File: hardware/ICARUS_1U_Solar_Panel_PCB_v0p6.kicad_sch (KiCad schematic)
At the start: 13 parts, among them J1 Molex_53398-0471

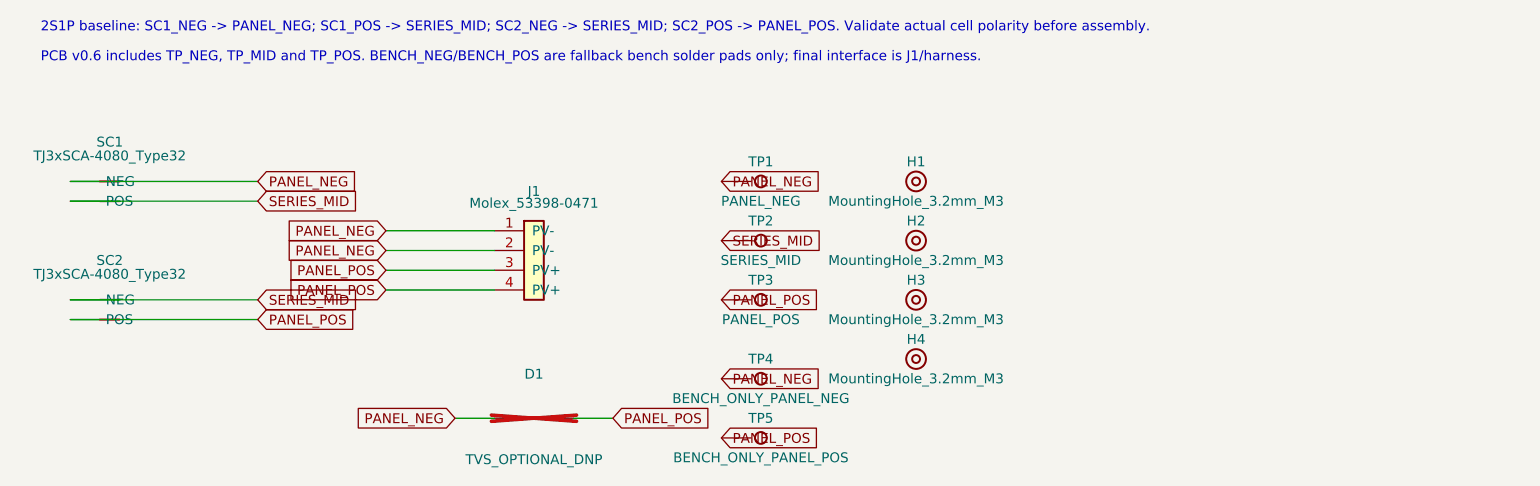
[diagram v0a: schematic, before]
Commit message: Repo hygiene: drop dead NC net, unify fp-lib-table, remove obsolete macOS reports
- Drop unused (net 4 "NC") from PCB (was declared but referenced by no
  pad/track).
- Point fp-lib-table entry for ICARUS_Connector at the unified
  hardware/footprints/ tree (matches ICARUS_Solar location).
- Update bench-pad note in schematic to use the real net names
  (BENCH_ONLY_PANEL_NEG/POS) instead of the old short forms.
- Delete the three .rpt files left from the aborted macOS DRC/ERC runs
  (DRC_v0p6.rpt, DRC_v0p6_layout_only.rpt, ERC_v0p6.rpt); current
  reports live in *_kicad10_win.rpt.

DRC parity remains clean (0 errors / 0 unconnected / 0 parity issues;
13 warnings = library-mismatch waived).

Co-Authored-By: Claude Opus 4.7 <noreply@anthropic.com>
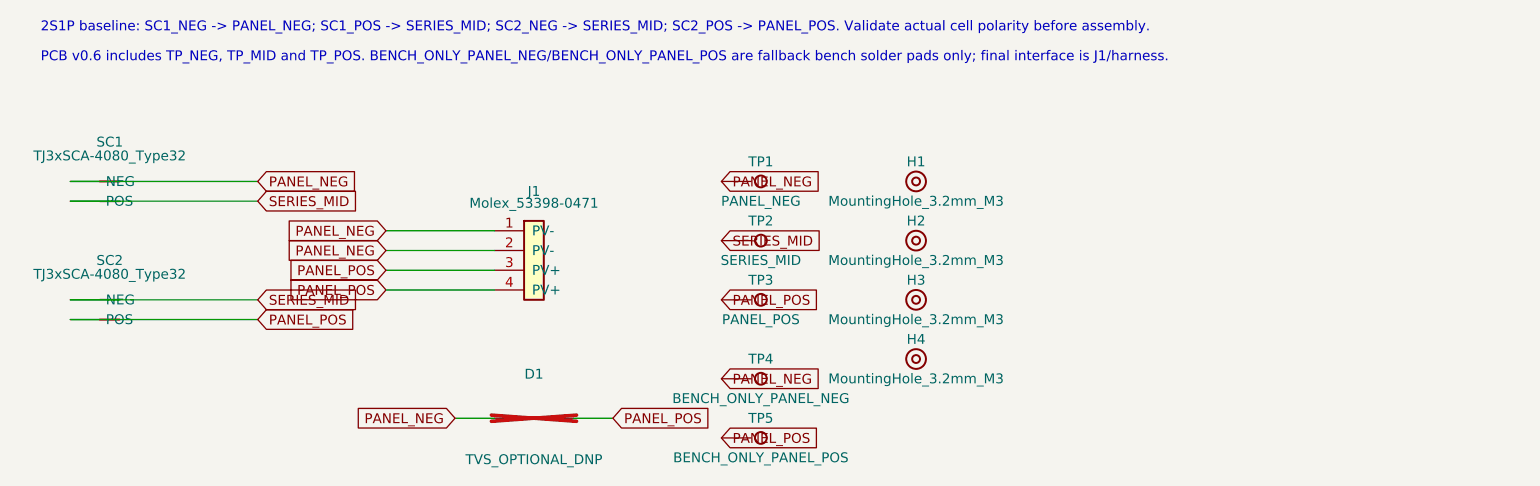
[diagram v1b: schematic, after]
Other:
- note added: "PCB v0.6 includes TP_NEG, TP_MID and TP_POS. BENCH_ONLY_PANEL_NEG/BENCH_ONLY_PANEL_POS are fallback bench solder pads only; final interface is J1/harness."
- note removed: "PCB v0.6 includes TP_NEG, TP_MID and TP_POS. BENCH_NEG/BENCH_POS are fallback bench solder pads only; final interface is J1/harness."
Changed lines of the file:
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@@
 			(global_label "PANEL_POS" (shape input) (at 154.94 109.22 0) (fields_autoplaced) (effects (font (size 1.27 1.27)) (justify left)))
 		(text "2S1P baseline: SC1_NEG -> PANEL_NEG; SC1_POS -> SERIES_MID; SC2_NEG -> SERIES_MID; SC2_POS -> PANEL_POS. Validate actual cell polarity before assembly." (at 67.31 57.15 0) (effects (font (size 1.27 1.27)) (justify left bottom)))
-	(text "PCB v0.6 includes TP_NEG, TP_MID and TP_POS. BENCH_NEG/BENCH_POS are fallback bench solder pads only; final interface is J1/harness." (at 67.31 61.0 0) (effects (font (size 1.27 1.27)) (justify left bottom)) (uuid "bench-note-v05"))
+	(text "PCB v0.6 includes TP_NEG, TP_MID and TP_POS. BENCH_ONLY_PANEL_NEG/BENCH_ONLY_PANEL_POS are fallback bench solder pads only; final interface is J1/harness." (at 67.31 61.0 0) (effects (font (size 1.27 1.27)) (justify left bottom)) (uuid "bench-note-v05"))
 	(symbol (lib_id "ICARUS:Solar_Cell_2Pin") (at 76.2 77.47 0) (unit 1) (exclude_from_sim no) (in_bom yes) (on_board yes) (dnp no)
 		(property "Reference" "SC1" (at 76.2 71.12 0) (effects (font (size 1.27 1.27))))
